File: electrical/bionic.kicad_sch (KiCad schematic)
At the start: 37 parts, among them J1 PWR, M1 N20, M2 N20, M3 N20, M4 N20, M5 N20, M6 N20, M7 N20, SW1 SW_SPST, U1 ESP32, U2 SAMD09, U3 CD4069, U4 CD4069, U5 LM338

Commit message: update(electrical/pcb): signal wiring Complete!!
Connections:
- net DIR1: now also U2.12 (15); no longer U2.8 (9)
- net DIR2: now also U2.11 (14); no longer U2.9 (10)
- net DIR4: now also U2.9 (10); no longer U2.11 (14)
- net DIR5: now also U2.8 (9); no longer U2.12 (15)
- net DIR7: now also D4.14 (AI1); no longer D4.12 (BI1)
- net ENA1: now also U1.22 (IO26); no longer U1.23 (IO25)
- net ENA5: now also U1.8 (IO5*); no longer U1.4 (IO2*)
- net ENA6: now also U1.6 (IO16/RX); no longer U1.7 (IO17/TX)
- net ENA7: now also U1.4 (IO2*); no longer U1.10 (IO19)
- net ENB1: now also U1.23 (IO25); no longer U1.22 (IO26)
- net ENB5: now also U1.7 (IO17/TX); no longer U1.5 (IO4)
- net ENB6: now also U1.5 (IO4); no longer U1.8 (IO5*)
- net ENB7: now also U1.3 (IO15*); no longer U1.15 (IO23)
- net M7+: now also D4.4 (A01); no longer D4.6 (B01)
- net M7-: now also D4.5 (A02); no longer D4.7 (B02)
- net M7B: now also D4.15 (AI2); no longer D4.11 (BI2)
- net PWM5: now also U1.15 (IO23); no longer U1.3 (IO15*)
- net PWM6: now also U1.10 (IO19); no longer U1.6 (IO16/RX)
- net PWM7: now also D4.16 (PWMA); no longer D4.10 (PWMB)
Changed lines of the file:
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@@
 	)
 	(no_connect
-		(at 265.43 25.4)
+		(at 245.11 38.1)
 	)
 	(no_connect
@@
 	)
 	(no_connect
+		(at 265.43 35.56)
+	)
+	(no_connect
 		(at 62.23 102.87)
 	)
@@
 	)
 	(no_connect
-		(at 265.43 27.94)
+		(at 245.11 40.64)
 	)
 	(no_connect
@@
 	)
 	(no_connect
-		(at 245.11 35.56)
-	)
-	(no_connect
-		(at 245.11 33.02)
-	)
-	(no_connect
 		(at 44.45 97.79)
 	)
@@
 	)
 	(no_connect
-		(at 265.43 30.48)
+		(at 265.43 40.64)
+	)
+	(no_connect
+		(at 265.43 38.1)
 	)
 	(wire
@@
 	(wire
 		(pts
-			(xy 36.83 40.64) (xy 30.48 40.64)
+			(xy 36.83 35.56) (xy 30.48 35.56)
 		)
 		(stroke
@@
 	(wire
 		(pts
-			(xy 76.2 49.53) (xy 82.55 49.53)
+			(xy 76.2 54.61) (xy 82.55 54.61)
 		)
 		(stroke
@@
 	(wire
 		(pts
-			(xy 76.2 57.15) (xy 82.55 57.15)
+			(xy 76.2 46.99) (xy 82.55 46.99)
 		)
 		(stroke
@@
 	(wire
 		(pts
-			(xy 238.76 38.1) (xy 245.11 38.1)
+			(xy 238.76 33.02) (xy 245.11 33.02)
 		)
 		(stroke
@@
 	(wire
 		(pts
-			(xy 265.43 40.64) (xy 271.78 40.64)
+			(xy 265.43 25.4) (xy 271.78 25.4)
 		)
 		(stroke
@@
 	(wire
 		(pts
-			(xy 271.78 38.1) (xy 265.43 38.1)
+			(xy 271.78 30.48) (xy 265.43 30.48)
 		)
 		(stroke
@@
 	(wire
 		(pts
-			(xy 36.83 35.56) (xy 30.48 35.56)
+			(xy 36.83 43.18) (xy 30.48 43.18)
 		)
 		(stroke
@@
 	(wire
 		(pts
-			(xy 36.83 33.02) (xy 30.48 33.02)
+			(xy 36.83 40.64) (xy 30.48 40.64)
 		)
 		(stroke
@@
 	(wire
 		(pts
-			(xy 30.48 60.96) (xy 36.83 60.96)
+			(xy 30.48 33.02) (xy 36.83 33.02)
 		)
 		(stroke
@@
 	(wire
 		(pts
-			(xy 238.76 40.64) (xy 245.11 40.64)
+			(xy 238.76 35.56) (xy 245.11 35.56)
 		)
 		(stroke
@@
 	(wire
 		(pts
-			(xy 76.2 46.99) (xy 82.55 46.99)
+			(xy 76.2 57.15) (xy 82.55 57.15)
 		)
 		(stroke
@@
 	(wire
 		(pts
-			(xy 76.2 54.61) (xy 82.55 54.61)
+			(xy 76.2 49.53) (xy 82.55 49.53)
 		)
 		(stroke
@@
 	(wire
 		(pts
-			(xy 30.48 30.48) (xy 36.83 30.48)
+			(xy 30.48 60.96) (xy 36.83 60.96)
 		)
 		(stroke
@@
 	(wire
 		(pts
-			(xy 30.48 38.1) (xy 36.83 38.1)
+			(xy 30.48 48.26) (xy 36.83 48.26)
 		)
 		(stroke
@@
 	(wire
 		(pts
-			(xy 36.83 43.18) (xy 30.48 43.18)
+			(xy 36.83 38.1) (xy 30.48 38.1)
 		)
 		(stroke
@@
 	(wire
 		(pts
-			(xy 30.48 48.26) (xy 36.83 48.26)
+			(xy 30.48 30.48) (xy 36.83 30.48)
 		)
 		(stroke
@@
 	(wire
 		(pts
-			(xy 271.78 35.56) (xy 265.43 35.56)
+			(xy 271.78 27.94) (xy 265.43 27.94)
 		)
 		(stroke
@@
 	)
 	(label "ENB7"
-		(at 30.48 60.96 0)
+		(at 30.48 30.48 0)
 		(fields_autoplaced yes)
 		(effects
@@
 	)
 	(label "DIR4"
-		(at 76.2 54.61 0)
+		(at 76.2 49.53 0)
 		(fields_autoplaced yes)
 		(effects
@@
 	)
 	(label "M7+"
-		(at 238.76 38.1 0)
+		(at 238.76 33.02 0)
 		(fields_autoplaced yes)
 		(effects
@@
 	)
 	(label "ENB1"
-		(at 71.12 40.64 180)
+		(at 71.12 43.18 180)
 		(fields_autoplaced yes)
 		(effects
@@
 	)
 	(label "PWM5"
-		(at 30.48 30.48 0)
+		(at 30.48 60.96 0)
 		(fields_autoplaced yes)
 		(effects
@@
 	)
 	(label "M7B"
-		(at 271.78 38.1 180)
+		(at 271.78 27.94 180)
 		(fields_autoplaced yes)
 		(effects
@@
 	)
 	(label "DIR2"
-		(at 76.2 49.53 0)
+		(at 76.2 54.61 0)
 		(fields_autoplaced yes)
 		(effects
@@
 	)
 	(label "PWM6"
-		(at 30.48 38.1 0)
+		(at 30.48 48.26 0)
 		(fields_autoplaced yes)
 		(effects
@@
 	)
 	(label "ENB6"
-		(at 30.48 43.18 0)
+		(at 30.48 35.56 0)
 		(fields_autoplaced yes)
 		(effects
@@
 	)
 	(label "ENA6"
-		(at 30.48 40.64 0)
+		(at 30.48 38.1 0)
 		(fields_autoplaced yes)
 		(effects
@@
 	)
 	(label "ENA5"
-		(at 30.48 33.02 0)
+		(at 30.48 43.18 0)
 		(fields_autoplaced yes)
 		(effects
@@
 	)
 	(label "PWM7"
-		(at 271.78 40.64 180)
+		(at 271.78 25.4 180)
 		(fields_autoplaced yes)
 		(effects
@@
 	)
 	(label "M7A"
-		(at 271.78 35.56 180)
+		(at 271.78 30.48 180)
 		(fields_autoplaced yes)
 		(effects
@@
 	)
 	(label "ENB5"
-		(at 30.48 35.56 0)
+		(at 30.48 40.64 0)
 		(fields_autoplaced yes)
 		(effects
@@
 	)
 	(label "ENA1"
-		(at 71.12 43.18 180)
+		(at 71.12 40.64 180)
 		(fields_autoplaced yes)
 		(effects
@@
 	)
 	(label "DIR5"
-		(at 76.2 57.15 0)
+		(at 76.2 46.99 0)
 		(fields_autoplaced yes)
 		(effects
@@
 	)
 	(label "ENA7"
-		(at 30.48 48.26 0)
+		(at 30.48 33.02 0)
 		(fields_autoplaced yes)
 		(effects
@@
 	)
 	(label "DIR1"
-		(at 76.2 46.99 0)
+		(at 76.2 57.15 0)
 		(fields_autoplaced yes)
 		(effects
@@
 	)
 	(label "M7-"
-		(at 238.76 40.64 0)
+		(at 238.76 35.56 0)
 		(fields_autoplaced yes)
 		(effects

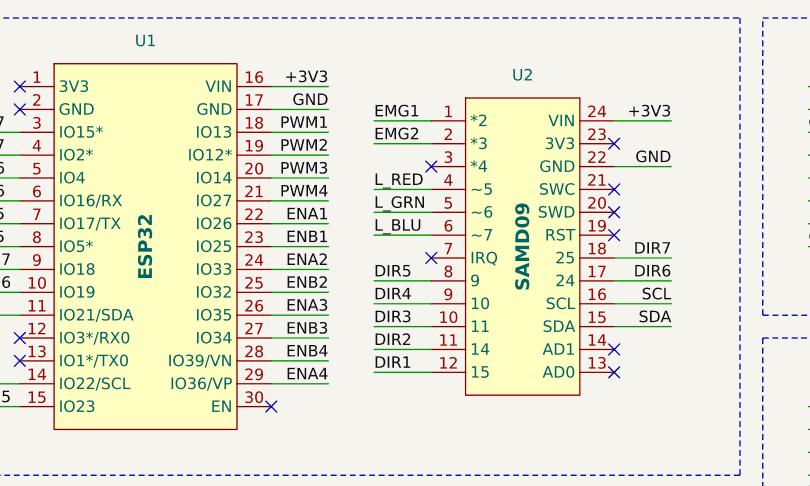
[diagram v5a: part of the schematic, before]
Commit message: update(electrical/pcb): DRC Passed! and Updated 3D-Models
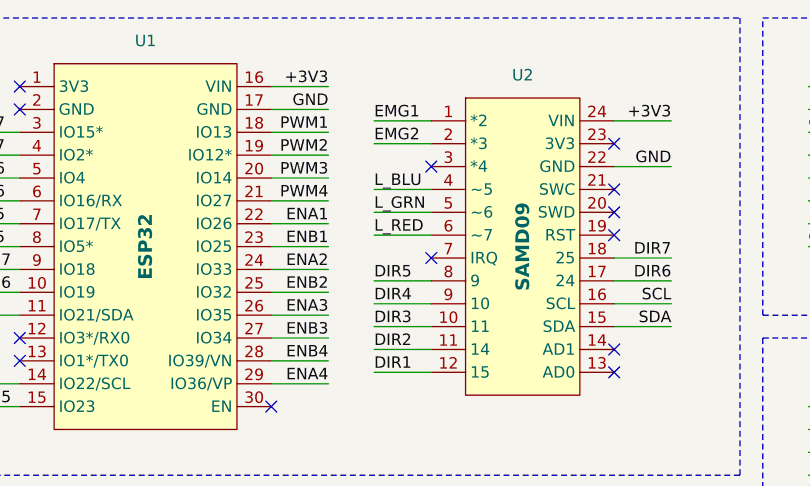
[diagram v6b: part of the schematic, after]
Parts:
- M1, M2, M3, M4, M5, M6, M7: footprint Connector_PinHeader_2.54mm:PinHeader_1x06_P2.54mm_Vertical -> bionic:JST_1x06_P2.54mm_Vertical
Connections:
- net L_BLU: now also U2.4 (~5); no longer U2.6 (~7)
- net L_RED: now also U2.6 (~7); no longer U2.4 (~5)
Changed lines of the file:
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@@
 	(wire
 		(pts
-			(xy 76.2 36.83) (xy 82.55 36.83)
+			(xy 76.2 41.91) (xy 82.55 41.91)
 		)
 		(stroke
@@
 	(wire
 		(pts
-			(xy 76.2 41.91) (xy 82.55 41.91)
+			(xy 76.2 36.83) (xy 82.55 36.83)
 		)
 		(stroke
@@
 	)
 	(label "L_RED"
-		(at 76.2 36.83 0)
+		(at 76.2 41.91 0)
 		(fields_autoplaced yes)
 		(effects
@@
 	)
 	(label "L_BLU"
-		(at 76.2 41.91 0)
+		(at 76.2 36.83 0)
 		(fields_autoplaced yes)
 		(effects
@@
 			)
 		)
-		(property "Footprint" "Connector_PinHeader_2.54mm:PinHeader_1x06_P2.54mm_Vertical"
+		(property "Footprint" "bionic:JST_1x06_P2.54mm_Vertical"
 			(at 133.35 88.9 0)
 			(effects
@@
 			)
 		)
-		(property "Footprint" "Connector_PinHeader_2.54mm:PinHeader_1x06_P2.54mm_Vertical"
+		(property "Footprint" "bionic:JST_1x06_P2.54mm_Vertical"
 			(at 160.02 88.9 0)
 			(effects
@@
 			)
 		)
-		(property "Footprint" "Connector_PinHeader_2.54mm:PinHeader_1x06_P2.54mm_Vertical"
+		(property "Footprint" "bionic:JST_1x06_P2.54mm_Vertical"
 			(at 133.35 66.04 0)
 			(effects
@@
 			)
 		)
-		(property "Footprint" "Connector_PinHeader_2.54mm:PinHeader_1x06_P2.54mm_Vertical"
+		(property "Footprint" "bionic:JST_1x06_P2.54mm_Vertical"
 			(at 213.36 66.04 0)
 			(effects
@@
 			)
 		)
-		(property "Footprint" "Connector_PinHeader_2.54mm:PinHeader_1x06_P2.54mm_Vertical"
+		(property "Footprint" "bionic:JST_1x06_P2.54mm_Vertical"
 			(at 160.02 66.04 0)
 			(effects
@@
 			)
 		)
-		(property "Footprint" "Connector_PinHeader_2.54mm:PinHeader_1x06_P2.54mm_Vertical"
+		(property "Footprint" "bionic:JST_1x06_P2.54mm_Vertical"
 			(at 186.69 66.04 0)
 			(effects
@@
 			)
 		)
-		(property "Footprint" "Connector_PinHeader_2.54mm:PinHeader_1x06_P2.54mm_Vertical"
+		(property "Footprint" "bionic:JST_1x06_P2.54mm_Vertical"
 			(at 186.69 88.9 0)
 			(effects

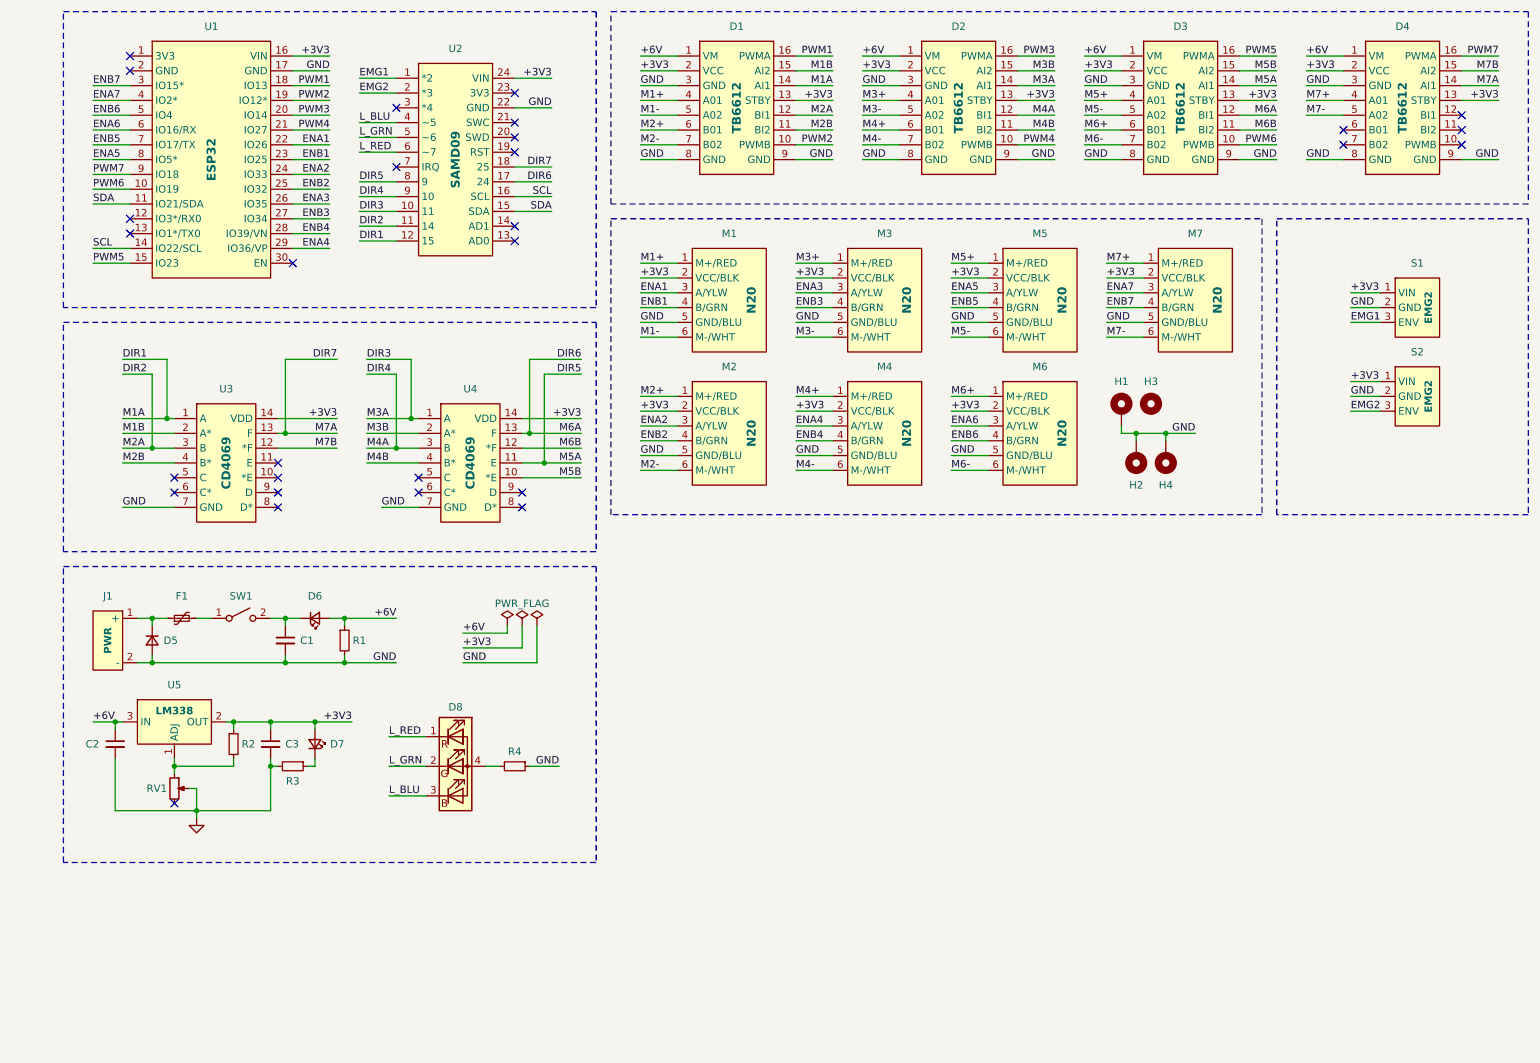
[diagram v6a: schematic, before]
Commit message: update(electrical/pcb): Updated Placement and Reduce Board
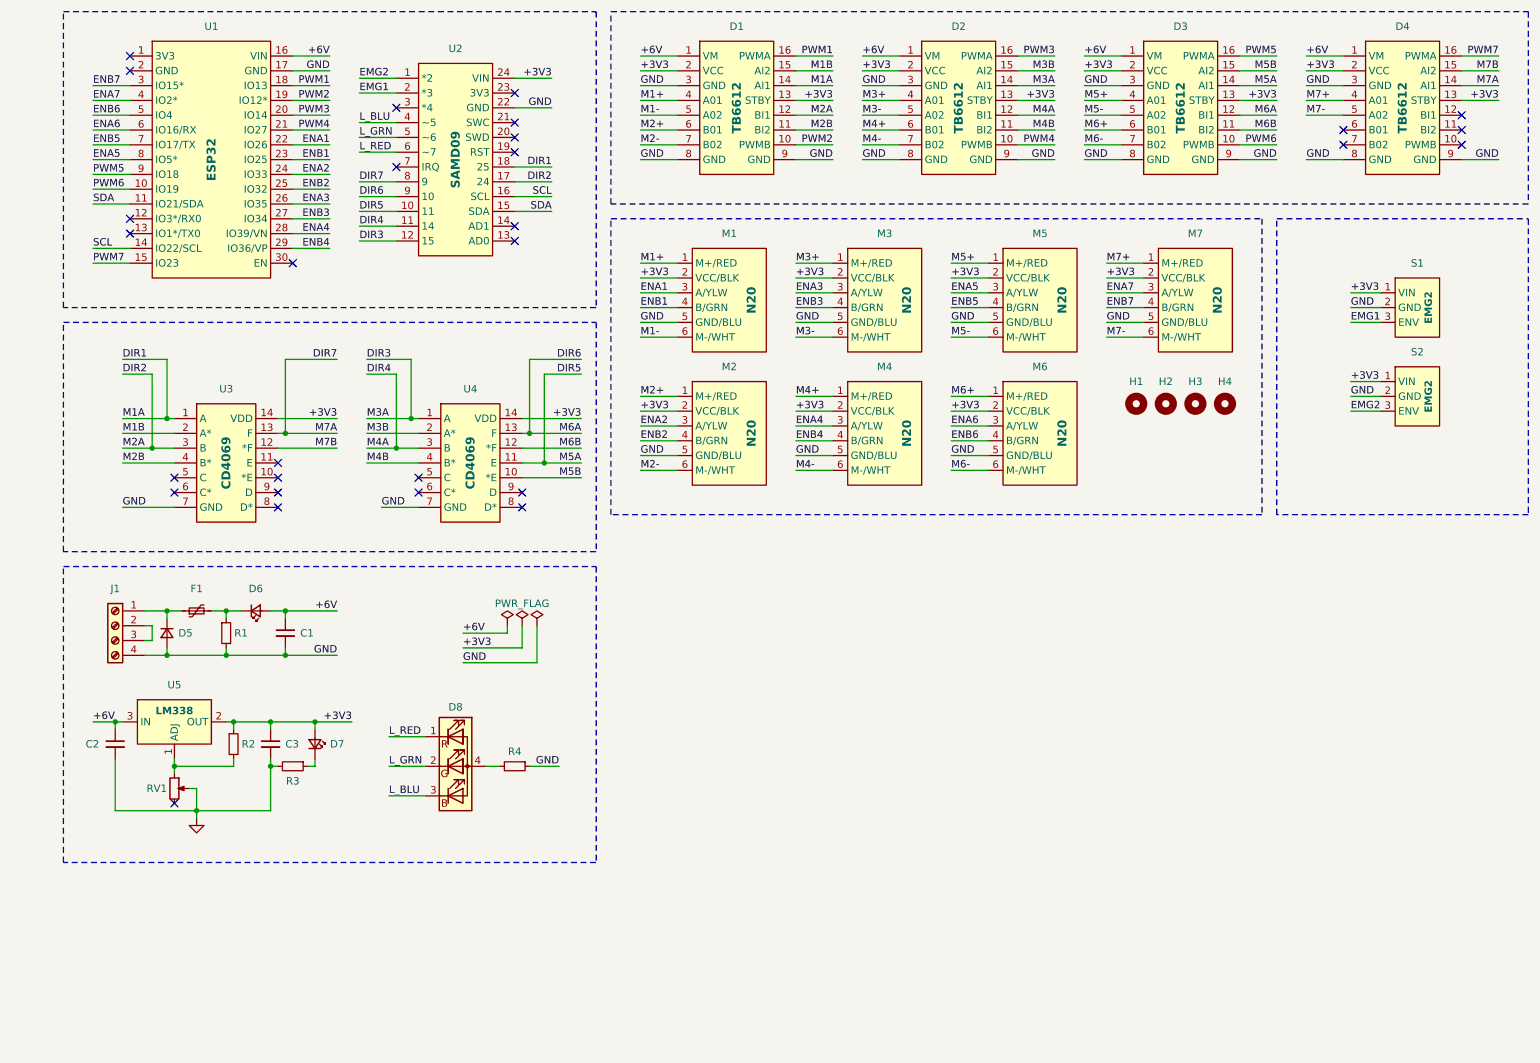
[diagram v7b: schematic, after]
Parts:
- removed H1, H2, H4: MountingHole_Pad, MountingHole:MountingHole_3.2mm_M3_Pad_Via, symbol Mechanical:MountingHole_Pad
- removed J1: PWR, TerminalBlock_Phoenix:TerminalBlock_Phoenix_MKDS-1,5-2-5.08_1x02_P5.08mm_Horizontal, symbol bionic:PWR
- removed SW1: SW_SPST, TerminalBlock_Phoenix:TerminalBlock_Phoenix_MKDS-1,5-2-5.08_1x02_P5.08mm_Horizontal, symbol Switch:SW_SPST
- added H1, H2, H4: MountingHole, MountingHole:MountingHole_3.2mm_M3, symbol Mechanical:MountingHole
- added J1: Screw_Terminal_01x04, TerminalBlock_Phoenix:TerminalBlock_Phoenix_MKDS-1,5-4-5.08_1x04_P5.08mm_Horizontal, symbol Connector:Screw_Terminal_01x04
- D6, D7: footprint LED_THT:LED_D5.0mm -> LED_THT:LED_D5.0mm_Horizontal_O1.27mm_Z3.0mm
- S1, S2: footprint Connector_PinHeader_2.54mm:PinHeader_1x03_P2.54mm_Vertical -> bionic:JST_1x03_P2.54mm_Vertical
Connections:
- net +3V3: no longer U1.16 (VIN)
- net +6V: now also C1.1, U1.16 (VIN); no longer R1.1
- net DIR1: now also U2.18 (25); no longer U2.12 (15)
- net DIR2: now also U2.17 (24); no longer U2.11 (14)
- net DIR3: now also U2.12 (15); no longer U2.10 (11)
- net DIR4: now also U2.11 (14); no longer U2.9 (10)
- net DIR5: now also U2.10 (11); no longer U2.8 (9)
- net DIR6: now also U2.9 (10); no longer U2.17 (24)
- net DIR7: now also U2.8 (9); no longer U2.18 (25)
- net EMG1: now also U2.2 (*3); no longer U2.1 (*2)
- net EMG2: now also U2.1 (*2); no longer U2.2 (*3)
- net ENA4: now also U1.28 (IO39/VN); no longer U1.29 (IO36/VP)
- net ENB4: now also U1.29 (IO36/VP); no longer U1.28 (IO39/VN)
- net GND: now also J1.4 (Pin_4)
- net PWM5: now also U1.9 (IO18); no longer U1.15 (IO23)
- net PWM7: now also U1.15 (IO23); no longer U1.9 (IO18)
- net at D6.1 (K): now also F1.2, R1.1; no longer C1.1
- net at D5.1 (K), F1.1: now also J1.1 (Pin_1)
- new net: J1.2 (Pin_2), J1.3 (Pin_3)
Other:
- moved on the sheet: C1, D6, H3, R1
